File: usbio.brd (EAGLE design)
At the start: 12.3 x 40.1 mm, 19 parts, among them U1 ATMEGA328P-MU-QFN32

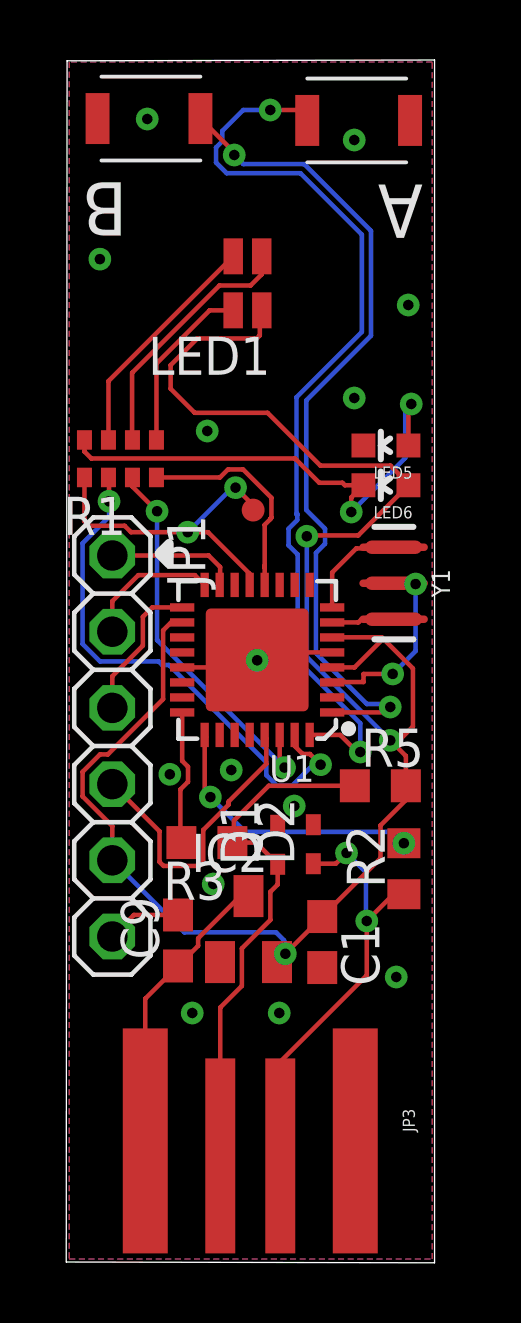
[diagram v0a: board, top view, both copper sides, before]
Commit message: Add LDO bypass jumper
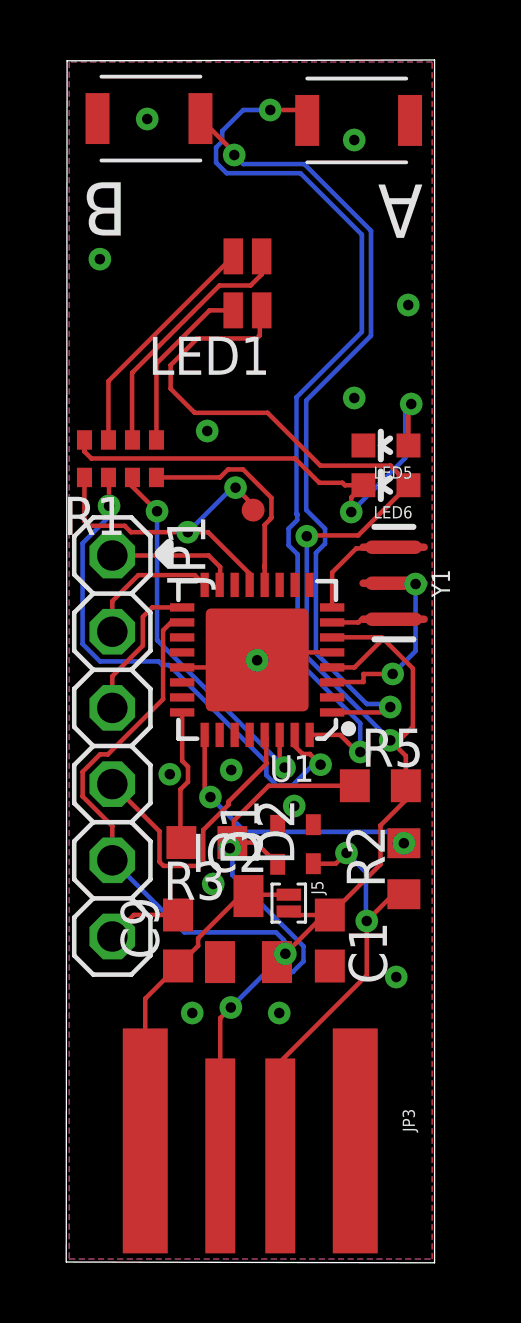
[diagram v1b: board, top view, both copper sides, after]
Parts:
- added J5: (no value), solderjumper:2.MED
- moved C1 0.26 mm to (8.79, 10.7)
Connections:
- net +3V3: now also J5.2
- net +5V: now also J5.1
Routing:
- net USB_D-: track 17.7 -> 20.4 mm, vias 0 -> 2
- net +3V3: track 61.5 -> 63.1 mm
- net +5V: track 9.75 -> 11.1 mm
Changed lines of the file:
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@@
 <layer number="17" name="Pads" color="2" fill="1" visible="yes" active="yes"/>
 <layer number="18" name="Vias" color="2" fill="1" visible="yes" active="yes"/>
-<layer number="19" name="Unrouted" color="6" fill="1" visible="no" active="yes"/>
+<layer number="19" name="Unrouted" color="6" fill="1" visible="yes" active="yes"/>
 <layer number="20" name="Dimension" color="24" fill="1" visible="no" active="yes"/>
 <layer number="21" name="tPlace" color="7" fill="1" visible="yes" active="yes"/>
 <layer number="22" name="bPlace" color="7" fill="1" visible="no" active="yes"/>
-<layer number="23" name="tOrigins" color="15" fill="1" visible="no" active="yes"/>
+<layer number="23" name="tOrigins" color="15" fill="1" visible="yes" active="yes"/>
 <layer number="24" name="bOrigins" color="15" fill="1" visible="no" active="yes"/>
 <layer number="25" name="tNames" color="7" fill="1" visible="no" active="yes"/>
@@
 <attribute name="VALUE" x="-1.639" y="24.82" size="1.27" layer="27" rot="R270"/>
 </element>
-<element name="C1" library="rcl" package="C0603" value="1uF" x="8.532" y="10.665" smashed="yes" rot="R270">
-<attribute name="NAME" x="9.167" y="11.3" size="1.27" layer="25" rot="R270"/>
-<attribute name="VALUE" x="6.627" y="11.3" size="1.27" layer="27" rot="R270"/>
+<element name="C1" library="rcl" package="C0603" value="1uF" x="8.786" y="10.7158" smashed="yes" rot="R270">
+<attribute name="NAME" x="9.421" y="11.3508" size="1.27" layer="25" rot="R270"/>
+<attribute name="VALUE" x="6.881" y="11.3508" size="1.27" layer="27" rot="R270"/>
 </element>
 <element name="IC2" library="MCP1700" package="SOT-23" value="" x="6.075" y="11.097" smashed="yes">
@@
 <attribute name="NAME" x="3.091" y="10.084" size="1.27" layer="25" rot="R90"/>
 <attribute name="VALUE" x="5.631" y="10.084" size="1.27" layer="27" rot="R90"/>
+</element>
+<element name="J5" library="solderjumper" package="2.MED" value="" x="7.4168" y="11.9634" smashed="yes" rot="R270">
+<attribute name="NAME" x="8.1668" y="12.7134" size="0.4064" layer="25" rot="R270"/>
+<attribute name="VALUE" x="6.1668" y="12.7134" size="0.4064" layer="27" rot="R270"/>
 </element>
 </elements>
@@
 <contactref element="IC2" pad="2"/>
 <wire x1="7.025" y1="9.997" x2="7.3025" y2="10.2745" width="0.1524" layer="1"/>
-<wire x1="7.3025" y1="10.2745" x2="8.532" y2="11.504" width="0.1524" layer="1"/>
-<wire x1="8.532" y1="11.504" x2="8.532" y2="11.515" width="0.1524" layer="1"/>
-<wire x1="8.532" y1="11.515" x2="10.4754" y2="13.4584" width="0.1524" layer="1"/>
-<wire x1="10.4754" y1="13.4584" x2="10.4754" y2="14.5536875" width="0.1524" layer="1"/>
+<wire x1="7.3025" y1="10.2745" x2="8.593909375" y2="11.565909375" width="0.1524" layer="1"/>
+<wire x1="8.593909375" y1="11.565909375" x2="8.786" y2="11.5658" width="0.1524" layer="1"/>
+<wire x1="8.786" y1="11.5658" x2="10.4754" y2="13.2552" width="0.1524" layer="1"/>
+<wire x1="10.4754" y1="13.2552" x2="10.4754" y2="14.5536875" width="0.1524" layer="1"/>
 <wire x1="11.32" y1="15.3982875" x2="11.32" y2="15.875" width="0.1524" layer="1"/>
 <wire x1="10.4754" y1="14.5536875" x2="11.32" y2="15.3982875" width="0.1524" layer="1"/>
@@
 <wire x1="3.4798" y1="29.1084" x2="4.2814" y2="28.3068" width="0.1524" layer="1"/>
 <wire x1="6.35" y1="30.7848" x2="4.3688" y2="30.7848" width="0.1524" layer="1"/>
+<contactref element="J5" pad="2"/>
+<wire x1="7.4168" y1="11.684" x2="7.535" y2="11.5658" width="0.1524" layer="1"/>
+<wire x1="7.535" y1="11.5658" x2="8.786" y2="11.5658" width="0.1524" layer="1"/>
 </signal>
 <signal name="ADCENA">
@@
 <contactref element="U1" pad="31"/>
 <wire x1="1.407" y1="26.152" x2="1.4262" y2="26.1328" width="0.1524" layer="1"/>
-<wire x1="1.4262" y1="26.1328" x2="1.4262" y2="25.3578" width="0.1524" layer="1"/>
-<via x="1.4262" y="25.3578" extent="1-16" drill="0.35"/>
+<wire x1="1.4262" y1="26.1328" x2="1.4262" y2="25.2054" width="0.1524" layer="1"/>
+<via x="1.4262" y="25.2054" extent="1-16" drill="0.35"/>
 <wire x1="0.5454" y1="20.599675" x2="1.125675" y2="20.0194" width="0.1524" layer="16"/>
-<wire x1="1.4262" y1="25.3578" x2="1.4262" y2="24.841125" width="0.1524" layer="16"/>
+<wire x1="1.4262" y1="25.2054" x2="1.4262" y2="24.841125" width="0.1524" layer="16"/>
 <wire x1="1.4262" y1="24.841125" x2="0.5454" y2="23.960325" width="0.1524" layer="16"/>
 <wire x1="0.5454" y1="23.960325" x2="0.5454" y2="20.599675" width="0.1524" layer="16"/>
@@
 <contactref element="JP3" pad="USB_M"/>
 <wire x1="5.238" y1="3.641" x2="5.134" y2="3.537" width="0.1524" layer="1"/>
-<wire x1="5.538" y1="13.981" x2="5.589" y2="13.981" width="0.1524" layer="1"/>
 <wire x1="5.589" y1="13.981" x2="6.324" y2="13.981" width="0.1524" layer="1"/>
 <wire x1="6.324" y1="13.981" x2="7.048" y2="13.257" width="0.1524" layer="1"/>
-<wire x1="6.8036" y1="11.4023125" x2="6.8036" y2="12.3386" width="0.1524" layer="1"/>
-<wire x1="5.134" y1="3.537" x2="5.134" y2="8.4827125" width="0.1524" layer="1"/>
-<wire x1="5.134" y1="8.4827125" x2="5.8536" y2="9.2023125" width="0.1524" layer="1"/>
-<wire x1="5.8536" y1="9.2023125" x2="5.8536" y2="10.4523125" width="0.1524" layer="1"/>
-<wire x1="5.8536" y1="10.4523125" x2="6.8036" y2="11.4023125" width="0.1524" layer="1"/>
-<wire x1="7.048" y1="12.583" x2="7.048" y2="13.257" width="0.1524" layer="1"/>
-<wire x1="6.8036" y1="12.3386" x2="7.048" y2="12.583" width="0.1524" layer="1"/>
 <wire x1="9.62" y1="15.875" x2="6.749" y2="15.875" width="0.1524" layer="1"/>
 <wire x1="5.589" y1="14.715" x2="5.589" y2="13.981" width="0.1524" layer="1"/>
 <wire x1="6.749" y1="15.875" x2="5.589" y2="14.715" width="0.1524" layer="1"/>
+<wire x1="5.134" y1="3.537" x2="5.134" y2="8.1312" width="0.1524" layer="1"/>
+<wire x1="5.134" y1="8.1312" x2="5.4864" y2="8.4836" width="0.1524" layer="1"/>
+<via x="5.4864" y="8.4836" extent="1-16" drill="0.35"/>
+<wire x1="7.55385" y1="9.6677" x2="7.9093" y2="10.02315" width="0.1524" layer="16"/>
+<wire x1="7.9093" y1="10.02315" x2="7.9093" y2="10.52585" width="0.1524" layer="16"/>
+<wire x1="7.9093" y1="10.52585" x2="5.5372" y2="12.89795" width="0.1524" layer="16"/>
+<wire x1="6.6705" y1="9.6677" x2="7.55385" y2="9.6677" width="0.1524" layer="16"/>
+<wire x1="5.4864" y1="8.4836" x2="6.6705" y2="9.6677" width="0.1524" layer="16"/>
+<wire x1="5.5372" y1="13.70545" x2="5.450625" y2="13.792025" width="0.1524" layer="16"/>
+<via x="5.450625" y="13.792025" extent="1-16" drill="0.35"/>
+<wire x1="5.538" y1="13.9302" x2="5.538" y2="13.981" width="0.1524" layer="1"/>
+<wire x1="5.538" y1="13.9302" x2="5.450625" y2="13.842825" width="0.1524" layer="1"/>
+<wire x1="5.450625" y1="13.842825" x2="5.450625" y2="13.792025" width="0.1524" layer="1"/>
+<wire x1="5.538" y1="13.981" x2="5.589" y2="13.981" width="0.1524" layer="1"/>
+<wire x1="5.5372" y1="12.89795" x2="5.5372" y2="13.70545" width="0.1524" layer="16"/>
 </signal>
 <signal name="USB_D+">
@@
 <wire x1="4.3964" y1="10.7916875" x2="5.8017125" y2="12.197" width="0.1524" layer="1"/>
 <wire x1="5.8017125" y1="12.197" x2="6.075" y2="12.197" width="0.1524" layer="1"/>
+<contactref element="J5" pad="1"/>
+<wire x1="7.4168" y1="12.2428" x2="6.1208" y2="12.2428" width="0.1524" layer="1"/>
+<wire x1="6.1208" y1="12.2428" x2="6.075" y2="12.197" width="0.1524" layer="1"/>
 </signal>
 </signals>

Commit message: Remove GND via too close to 5V
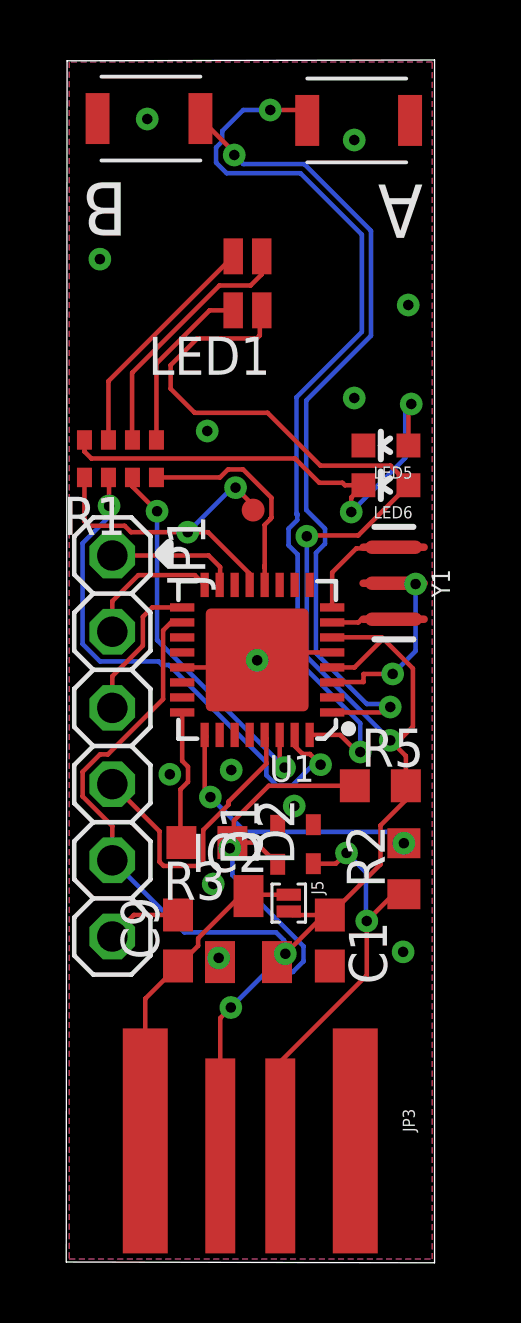
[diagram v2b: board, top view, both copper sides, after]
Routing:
- net GND: vias 16 -> 15
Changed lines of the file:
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@@
 <layer number="18" name="Vias" color="2" fill="1" visible="yes" active="yes"/>
 <layer number="19" name="Unrouted" color="6" fill="1" visible="yes" active="yes"/>
-<layer number="20" name="Dimension" color="24" fill="1" visible="no" active="yes"/>
+<layer number="20" name="Dimension" color="24" fill="1" visible="yes" active="yes"/>
 <layer number="21" name="tPlace" color="7" fill="1" visible="yes" active="yes"/>
-<layer number="22" name="bPlace" color="7" fill="1" visible="no" active="yes"/>
+<layer number="22" name="bPlace" color="7" fill="1" visible="yes" active="yes"/>
 <layer number="23" name="tOrigins" color="15" fill="1" visible="yes" active="yes"/>
-<layer number="24" name="bOrigins" color="15" fill="1" visible="no" active="yes"/>
+<layer number="24" name="bOrigins" color="15" fill="1" visible="yes" active="yes"/>
 <layer number="25" name="tNames" color="7" fill="1" visible="no" active="yes"/>
 <layer number="26" name="bNames" color="7" fill="1" visible="no" active="yes"/>
 <layer number="27" name="tValues" color="7" fill="1" visible="no" active="yes"/>
 <layer number="28" name="bValues" color="7" fill="1" visible="no" active="yes"/>
-<layer number="29" name="tStop" color="7" fill="3" visible="yes" active="yes"/>
-<layer number="30" name="bStop" color="7" fill="6" visible="yes" active="yes"/>
+<layer number="29" name="tStop" color="7" fill="3" visible="no" active="yes"/>
+<layer number="30" name="bStop" color="7" fill="6" visible="no" active="yes"/>
 <layer number="31" name="tCream" color="7" fill="4" visible="no" active="yes"/>
 <layer number="32" name="bCream" color="7" fill="5" visible="no" active="yes"/>
@@
 <vertex x="0.1" y="40"/>
 </polygon>
-<via x="7.1" y="8.3" extent="1-16" drill="0.35"/>
-<via x="11" y="9.5" extent="1-16" drill="0.35"/>
-<via x="4.2" y="8.3" extent="1-16" drill="0.35"/>
+<via x="11.2286" y="10.3382" extent="1-16" drill="0.35"/>
 <via x="11.4" y="31.9" extent="1-16" drill="0.35"/>
 <via x="9.6" y="28.8" extent="1-16" drill="0.35"/>
@@
 <via x="6.3636" y="20.0576" extent="1-16" drill="0.35"/>
 <via x="3.4522" y="16.2576" extent="1-16" drill="0.35"/>
+<via x="5.0818" y="10.135" extent="1-16" drill="0.35"/>
 </signal>
 <signal name="LED">
